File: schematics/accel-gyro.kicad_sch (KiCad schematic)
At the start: 2 parts, among them U2 LSM6DSOXTR

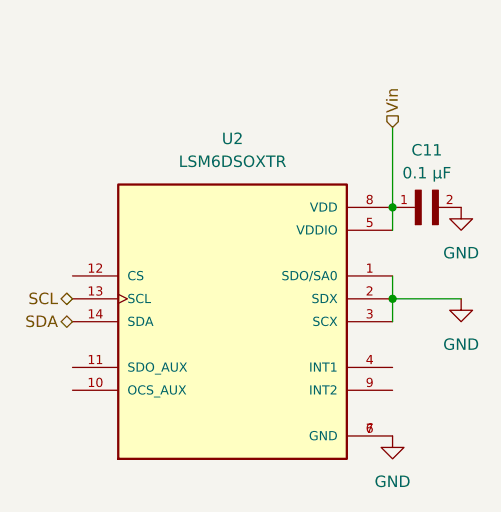
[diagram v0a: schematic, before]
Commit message: I2C fixes (level shifter, pull-up resistors); short-circuit typo fix
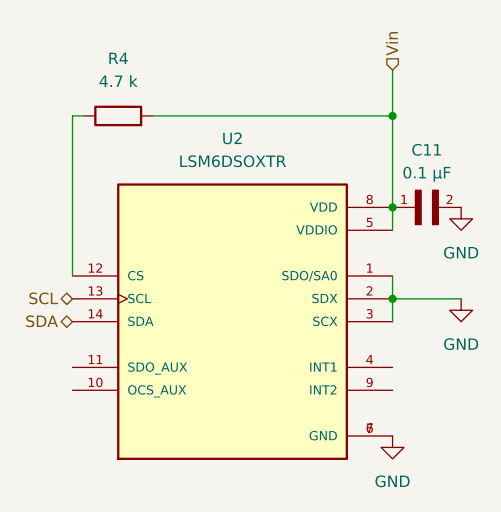
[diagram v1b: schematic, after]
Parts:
- added R4: 4.7 k, symbol Device:R
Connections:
- net Vin: now also R4.2
- net at U2.12 (CS): now also R4.1
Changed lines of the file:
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@@
+	)
+	(junction
+		(at 165.1 71.12)
+		(diameter 0)
+		(color 0 0 0 0)
 	)
 	(junction
@@
 	(wire
 		(pts
-			(xy 165.1 72.39) (xy 165.1 81.28)
+			(xy 165.1 71.12) (xy 165.1 81.28)
 		)
 		(stroke
@@
 	(wire
 		(pts
-			(xy 165.1 91.44) (xy 165.1 93.98)
+			(xy 165.1 66.04) (xy 165.1 71.12)
 		)
 		(stroke
@@
 	(wire
 		(pts
-			(xy 165.1 91.44) (xy 172.72 91.44)
+			(xy 165.1 91.44) (xy 165.1 93.98)
 		)
 		(stroke
@@
 	(wire
 		(pts
-			(xy 165.1 88.9) (xy 165.1 91.44)
+			(xy 165.1 91.44) (xy 172.72 91.44)
 		)
 		(stroke
@@
 	(wire
 		(pts
-			(xy 165.1 81.28) (xy 165.1 83.82)
+			(xy 165.1 88.9) (xy 165.1 91.44)
 		)
 		(stroke
@@
 		)
 	)
+	(wire
+		(pts
+			(xy 165.1 81.28) (xy 165.1 83.82)
+		)
+		(stroke
+			(width 0)
+			(type default)
+		)
+	)
+	(wire
+		(pts
+			(xy 138.43 71.12) (xy 165.1 71.12)
+		)
+		(stroke
+			(width 0)
+			(type default)
+		)
+	)
+	(wire
+		(pts
+			(xy 129.54 71.12) (xy 130.81 71.12)
+		)
+		(stroke
+			(width 0)
+			(type default)
+		)
+	)
+	(wire
+		(pts
+			(xy 129.54 88.9) (xy 129.54 71.12)
+		)
+		(stroke
+			(width 0)
+			(type default)
+		)
+	)
 	(hierarchical_label "Vin"
 		(shape input)
-		(at 165.1 72.39 90)
+		(at 165.1 66.04 90)
 		(effects
 			(font
@@
 			)
 		)
+		(property "SNAPEDA_PN" ""
+			(at 147.32 93.98 0)
+			(effects
+				(font
+					(size 1.27 1.27)
+				)
+				(hide yes)
+			)
+		)
+		(property "Sim.Device" ""
+			(at 147.32 93.98 0)
+			(effects
+				(font
+					(size 1.27 1.27)
+				)
+				(hide yes)
+			)
+		)
+		(property "Sim.Pins" ""
+			(at 147.32 93.98 0)
+			(effects
+				(font
+					(size 1.27 1.27)
+				)
+				(hide yes)
+			)
+		)
+		(property "Sim.Type" ""
+			(at 147.32 93.98 0)
+			(effects
+				(font
+					(size 1.27 1.27)
+				)
+				(hide yes)
+			)
+		)
 		(pin "9"
 		)
@@
 				(path "/2c1d9222-af16-428b-85a5-a3d420373d70/cfd34f19-b9c8-43fa-a529-56c363000dae"
 					(reference "U2")
+					(unit 1)
+				)
+			)
+		)
+	)
+	(symbol
+		(lib_id "Device:R")
+		(at 134.62 71.12 90)
+		(unit 1)
+		(exclude_from_sim no)
+		(in_bom yes)
+		(on_board yes)
+		(dnp no)
+		(fields_autoplaced yes)
+		(property "Reference" "R4"
+			(at 134.62 64.77 90)
+			(effects
+				(font
+					(size 1.27 1.27)
+				)
+			)
+		)
+		(property "Value" "4.7 k"
+			(at 134.62 67.31 90)
+			(effects
+				(font
+					(size 1.27 1.27)
+				)
+			)
+		)
+		(property "Footprint" ""
+			(at 134.62 72.898 90)
+			(effects
+				(font
+					(size 1.27 1.27)
+				)
+				(hide yes)
+			)
+		)
+		(property "Datasheet" "~"
+			(at 134.62 71.12 0)
+			(effects
+				(font
+					(size 1.27 1.27)
+				)
+				(hide yes)
+			)
+		)
+		(property "Description" "Resistor"
+			(at 134.62 71.12 0)
+			(effects
+				(font
+					(size 1.27 1.27)
+				)
+				(hide yes)
+			)
+		)
+		(pin "2"
+		)
+		(pin "1"
+		)
+		(instances
+			(project ""
+				(path "/2c1d9222-af16-428b-85a5-a3d420373d70/cfd34f19-b9c8-43fa-a529-56c363000dae"
+					(reference "R4")
 					(unit 1)
 				)
@@
 				(hide yes)
 			)
+		)
+		(property "SNAPEDA_PN" ""
+			(at 167.64 81.28 0)
+			(effects
+				(font
+					(size 1.27 1.27)
+				)
+				(hide yes)
+			)
+		)
+		(property "Sim.Device" ""
+			(at 167.64 81.28 0)
+			(effects
+				(font
+					(size 1.27 1.27)
+				)
+				(hide yes)
+			)
+		)
+		(property "Sim.Pins" ""
+			(at 167.64 81.28 0)
+			(effects
+				(font
+					(size 1.27 1.27)
+				)
+				(hide yes)
+			)
+		)
+		(property "Sim.Type" ""
+			(at 167.64 81.28 0)
+			(effects
+				(font
+					(size 1.27 1.27)
+				)
+				(hide yes)
+			)
